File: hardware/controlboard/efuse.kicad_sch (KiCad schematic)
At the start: 15 parts, among them U2 TPS25963x

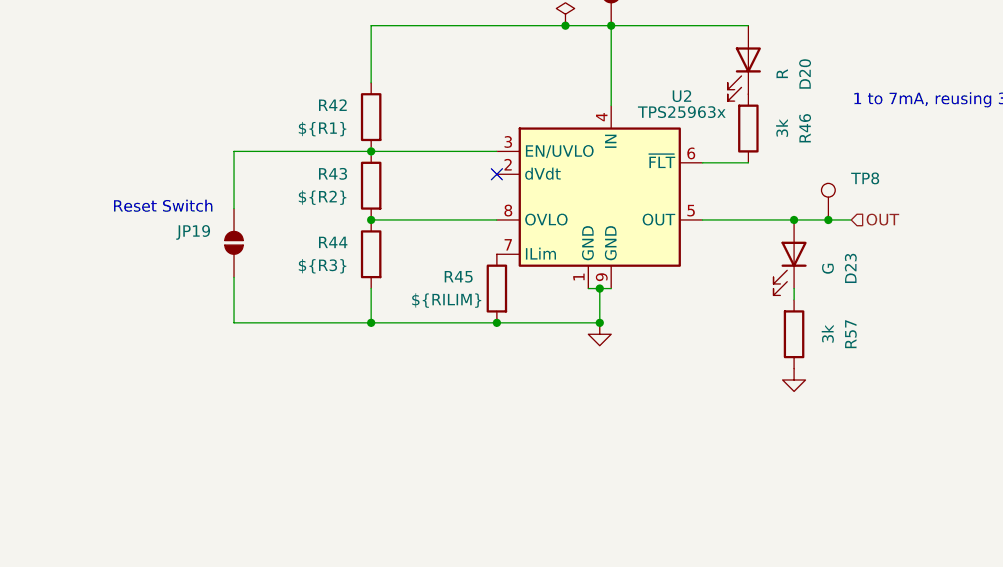
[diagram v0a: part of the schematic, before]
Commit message: Revert controlboard to June 12th 2024
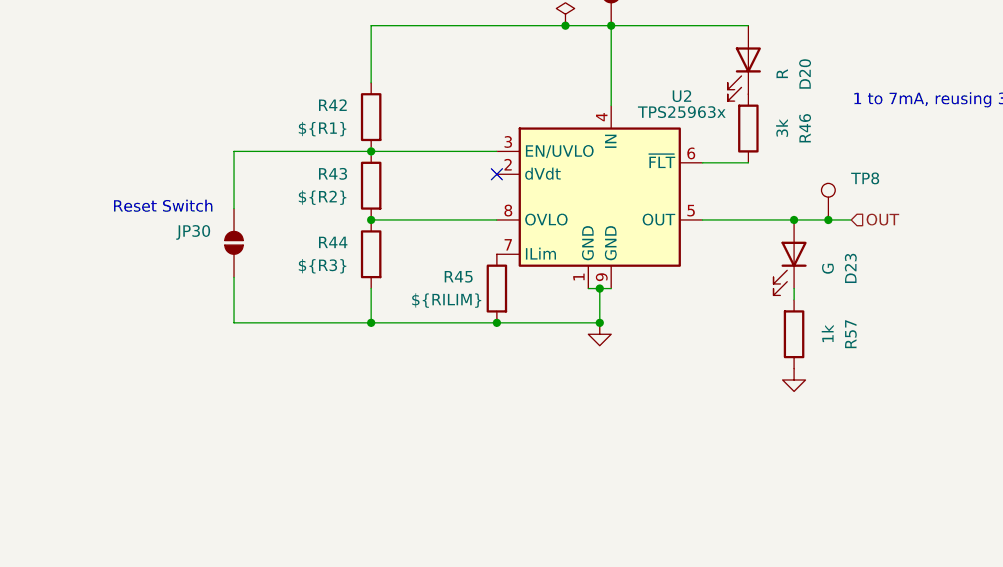
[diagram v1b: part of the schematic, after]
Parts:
- R57: value 3k -> 1k
- renumbered JP19 to JP30
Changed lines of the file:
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@@
 			)
 		)
-		(property "Value" "3k"
+		(property "Value" "1k"
 			(at 146.05 95.25 90)
 			(effects
@@
 		(on_board yes)
 		(dnp no)
-		(property "Reference" "JP19"
+		(property "Reference" "JP30"
 			(at 77.47 83.8199 90)
 			(effects
@@
 		(instances
 			(project "controlboard"
+				(path "/2797250d-6fee-4769-b4dd-0e20ce4f0941/5fab4b81-761e-4fae-b113-00364a75fd9a/c4ae39fe-dfab-4842-91d5-7d80cdea31e1"
+					(reference "JP30")
+					(unit 1)
+				)
 				(path "/2797250d-6fee-4769-b4dd-0e20ce4f0941/5fab4b81-761e-4fae-b113-00364a75fd9a/6730c4ed-849e-4137-aae0-c93a08939ea9"
 					(reference "JP19")
@@
 					(unit 1)
 				)
-				(path "/2797250d-6fee-4769-b4dd-0e20ce4f0941/5fab4b81-761e-4fae-b113-00364a75fd9a/c4ae39fe-dfab-4842-91d5-7d80cdea31e1"
-					(reference "JP30")
-					(unit 1)
-				)
